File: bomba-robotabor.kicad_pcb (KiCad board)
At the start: 2 copper layers, 51 parts, among them U1 74HC03, U2 74HCT08, U3 L4904

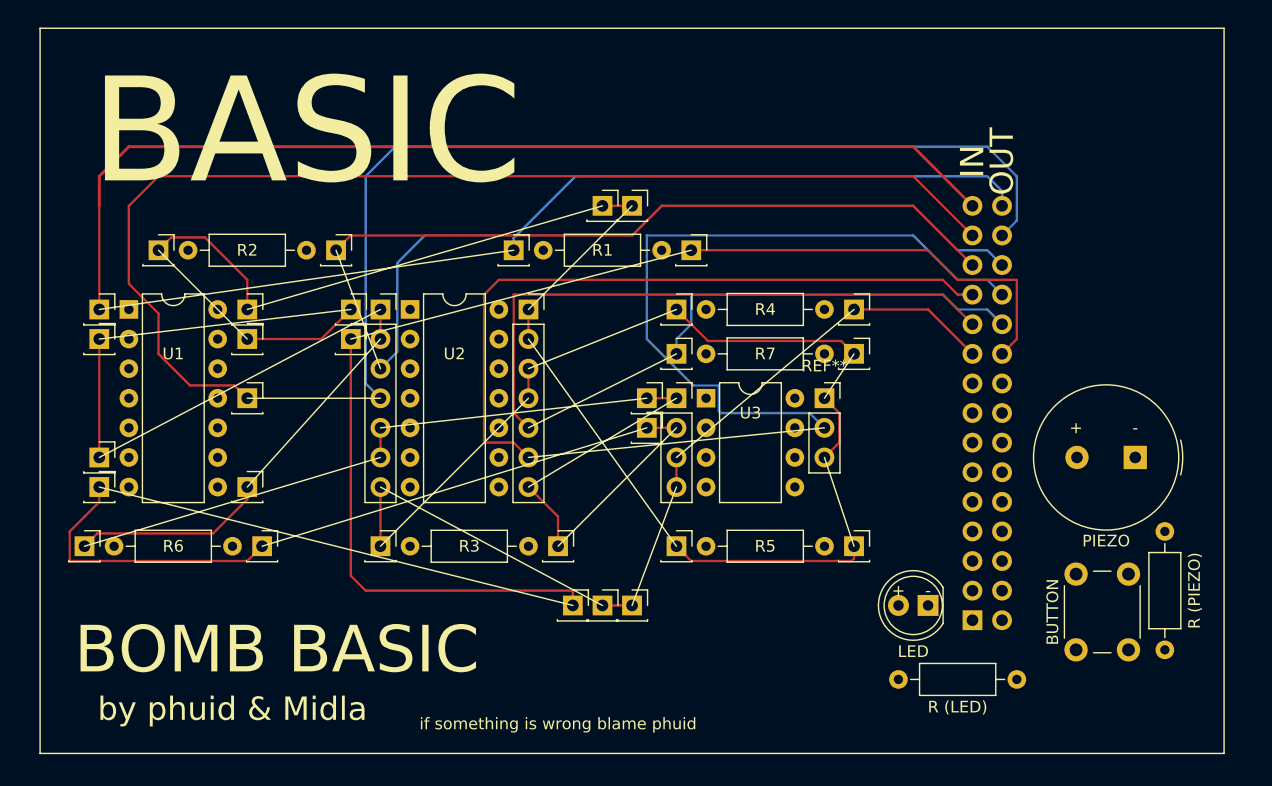
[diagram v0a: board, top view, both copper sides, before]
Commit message: control components connected
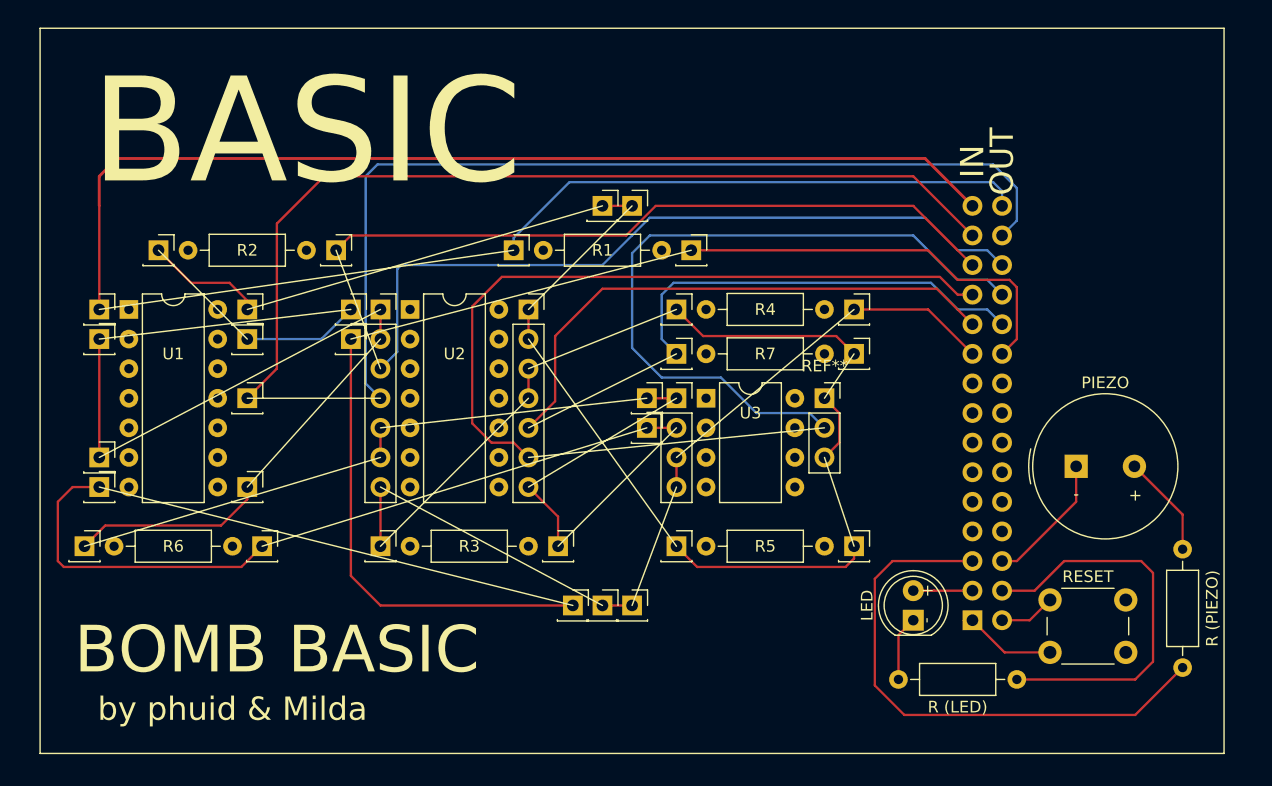
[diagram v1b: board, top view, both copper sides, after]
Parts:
- moved PIEZO 5.13 mm to (200.7, 70.6), turned to 0 degrees
- moved RESET 4.83 mm to (198.4, 82.1), turned to 0 degrees
- moved R (PIEZO) 2.16 mm to (209.8, 87.9)
- moved LED 1.80 mm to (186.7, 83.8), turned to 90 degrees
- renumbered BUTTON to RESET
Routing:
- net (no net): track 885.7 -> 989.5 mm
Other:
- board text added: "by phuid & Milda"
- board text removed: "by phuid & Midla"
- board text removed: "if something is wrong blame phuid"

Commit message: Add files via upload
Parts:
- moved PIEZO 6.39 mm to (207.0, 69.8), turned to 180 degrees
- moved RESET 4.73 mm to (202.9, 80.6), turned to -90 degrees
- turned LED to 180 degrees
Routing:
- net (no net): track 989.5 -> 928.4 mm

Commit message: slight adujstments
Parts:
- moved   4.83 mm to (120.4, 77.5)
- moved   4.83 mm to (135.6, 77.5)
- moved R6 4.83 mm to (133.1, 77.5)
- moved LED 1.27 mm to (185.4, 83.8), turned to 90 degrees
- moved R (PIEZO) 1.02 mm to (209.8, 86.9)
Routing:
- net (no net): track 928.4 -> 910.7 mm
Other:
- board text added: "CABLE"
- board text removed: "IN"
- board text removed: "OUT"

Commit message: potentio added, clarity improvement
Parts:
- added REF**: Potentiometer_ACP_CA9-V10_Vertical, Potentiometer_THT:Potentiometer_ACP_CA9-V10_Vertical, F.Cu at (207.2, 60.9)
- moved LED 2.03 mm to (185.4, 85.9)
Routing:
- net (no net): track 910.7 -> 997.9 mm
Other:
- board text added: "DO NOT TOUCH"

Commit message: part list added, bunch of junk
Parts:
- removed the PIEZO at (207.0, 69.8)
- added PIEZO: Buzzer_12x9.5RM7.6, Buzzer_Beeper:Buzzer_12x9.5RM7.6, F.Cu at (201.2, 69.3)
- 1kR: renamed from R (PIEZO)
- moved R (LED) 1.80 mm to (193.8, 89.2)
- moved   1.78 mm to (141.0, 79.2)
- moved   1.78 mm to (156.2, 79.2)
- moved R3 1.78 mm to (153.7, 79.2)
- moved LED 1.52 mm to (183.9, 85.9)
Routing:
- net (no net): track 997.9 -> 1000.1 mm
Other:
- board text removed: "+"
- board text removed: "-"

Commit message: part list propably finalized
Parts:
- removed the REF** at (207.2, 60.9)
- added REF**: SW_DIP_SPSTx04_Slide_6.7x11.72mm_W7.62mm_P2.54mm_LowProfile, Button_Switch_THT:SW_DIP_SPSTx04_Slide_6.7x11.72mm_W7.62mm_P2.54mm_LowProfile, F.Cu at (197.1, 71.1)
- moved PIEZO 9.96 mm to (200.2, 59.4)
- moved RESET 9.77 mm to (198.2, 89.1), turned to 90 degrees
- moved 1kR 2.03 mm to (207.8, 86.9)
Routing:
- net (no net): track 1000.1 -> 985.6 mm

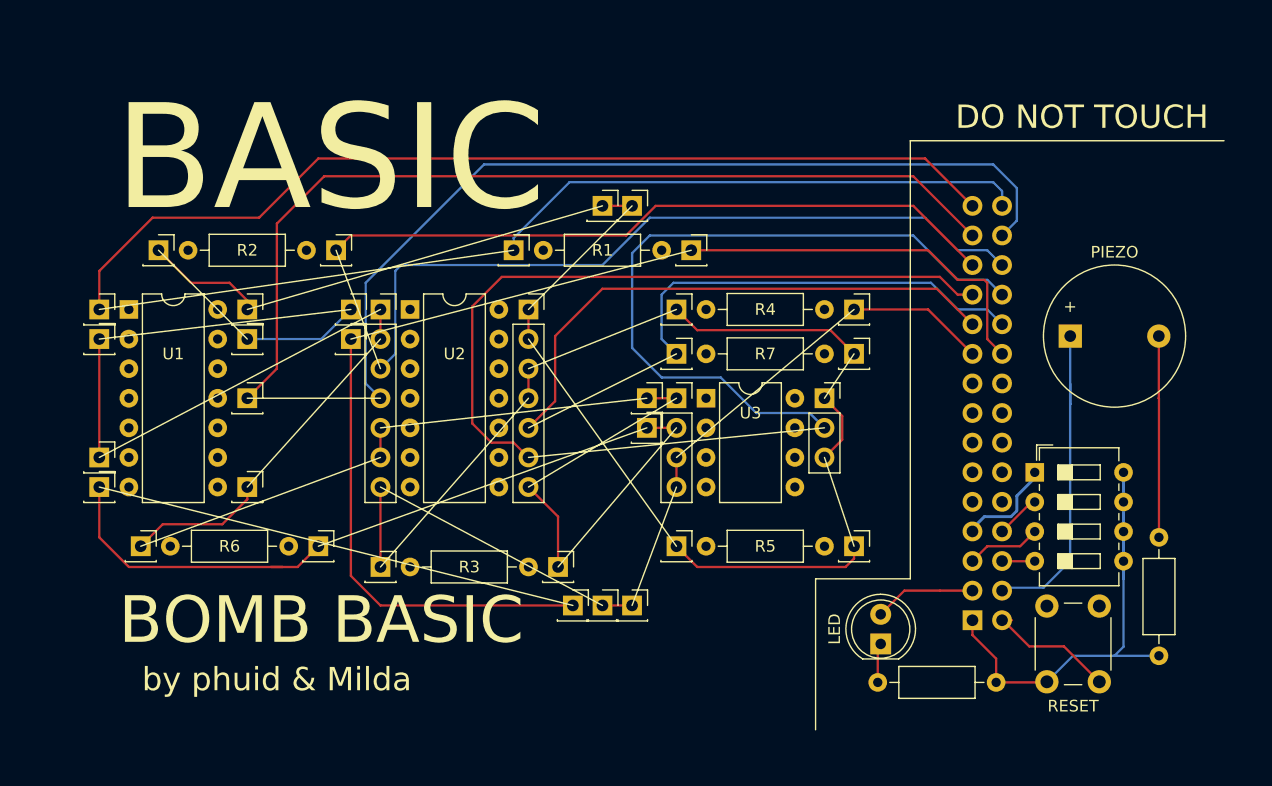
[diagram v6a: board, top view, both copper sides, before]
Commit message: converted to single ground, part list propably doneish
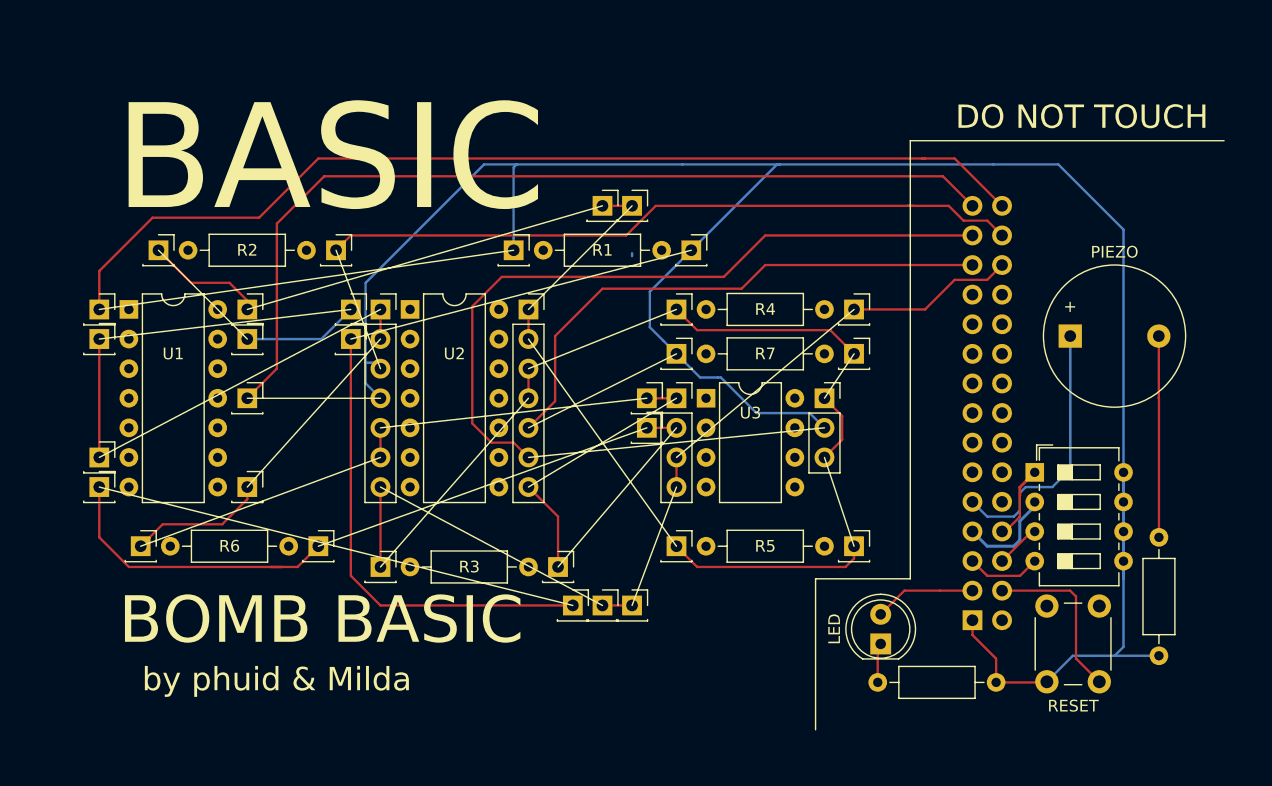
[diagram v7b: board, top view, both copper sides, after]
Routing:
- net (no net): track 985.6 -> 826.1 mm

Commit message: outline added, part list corrected, resistor tag added, continuity check
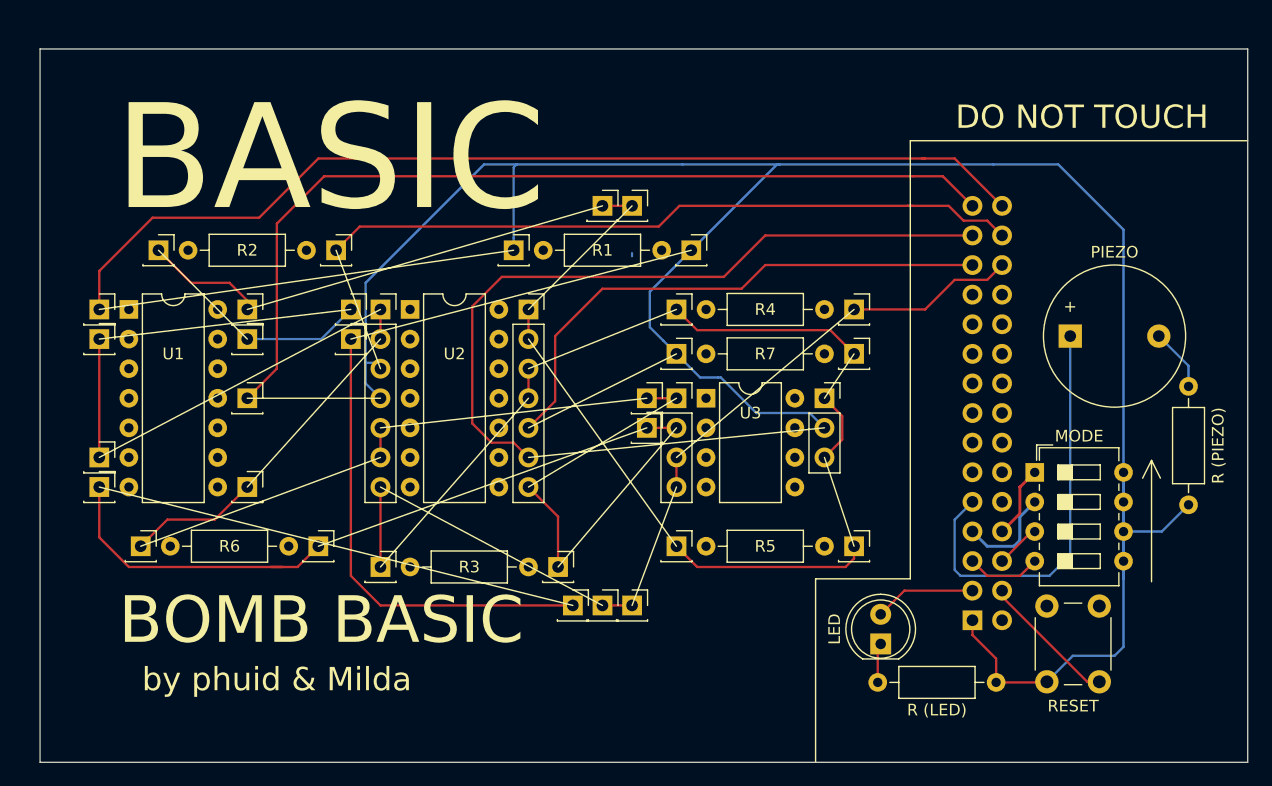
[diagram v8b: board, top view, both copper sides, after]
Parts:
- R (PIEZO): renamed from 1kR
- moved R (PIEZO) 13.2 mm to (210.3, 73.9)
- renumbered REF** to MODE
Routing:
- net (no net): track 826.1 -> 825.4 mm
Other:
- board outline added: 103.6 x 61.2 mm
